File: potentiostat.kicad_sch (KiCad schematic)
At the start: 30 parts, among them J1 Conn_01x01_Socket, J2 Conn_01x01_Socket, SW1 SW_Push, SW2 SW_Push, U1 ESP32-WROOM-32, U2 AD9833xRM, U3 TLV2372ID, U4 AMS1117-3.3, Y2 25MHz

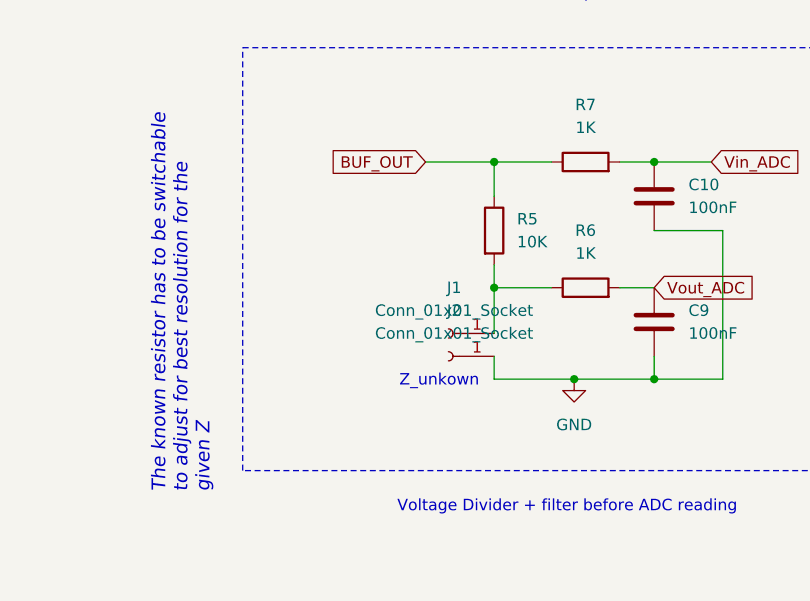
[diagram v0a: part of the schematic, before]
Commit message: dip switch added
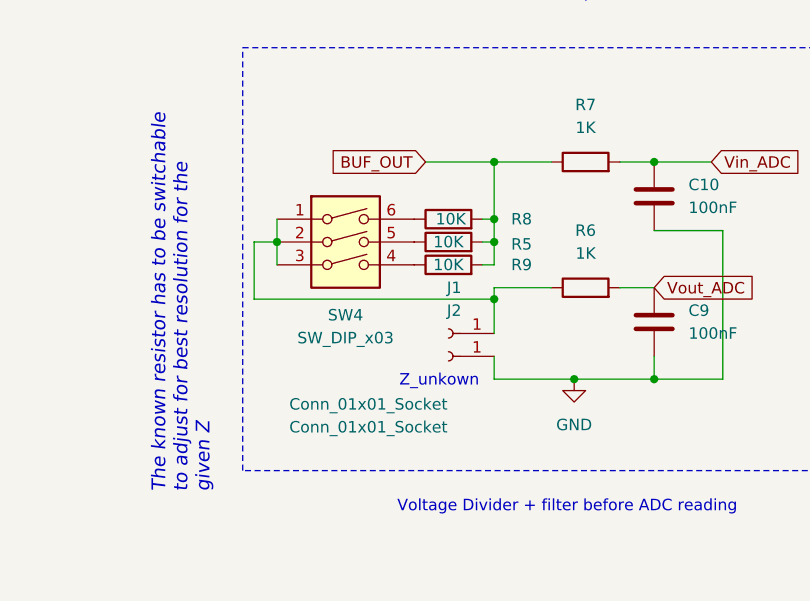
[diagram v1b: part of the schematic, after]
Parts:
- added R8, R9: 10K, Resistor_SMD:R_0603_1608Metric, symbol Device:R
- added SW4: SW_DIP_x03, Button_Switch_SMD:SW_DIP_SPSTx03_Slide_KingTek_DSHP03TJ_W5.25mm_P1.27mm_JPin, symbol Switch:SW_DIP_x03
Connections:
- net BUF_OUT: now also R5.2, R8.2, R9.2; no longer R5.1
- net at J1.1 (Pin_1), R6.1: now also SW4.1, SW4.2, SW4.3; no longer R5.2
- new net: R8.1, SW4.6
- new net: R9.1, SW4.4
- new net: R5.1, SW4.5
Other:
- moved on the sheet: R5

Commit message: debugging pins
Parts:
- added J3: Conn_01x03_Pin, Connector_PinHeader_2.54mm:PinHeader_1x03_P2.54mm_Horizontal, symbol Connector:Conn_01x03_Pin
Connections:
- net GND: now also J3.1 (Pin_1)
- net RX: now reaches U1.34 (RXD0/IO3)
- net RX: now also J3.2 (Pin_2)
- net TX: now reaches U1.35 (TXD0/IO1)
- net TX: now also J3.3 (Pin_3)
- no-connect marks 29 -> 27
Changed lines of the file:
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@@
 	)
 	(rectangle
+		(start 139.7 105.41)
+		(end 157.48 128.27)
+		(stroke
+			(width 0)
+			(type dash)
+		)
+		(fill
+			(type none)
+		)
+	)
+	(rectangle
 		(start 24.13 69.85)
 		(end 67.31 95.25)
@@
 		)
 	)
+	(rectangle
+		(start 69.85 71.12)
+		(end 91.44 93.98)
+		(stroke
+			(width 0)
+			(type dash)
+		)
+		(fill
+			(type none)
+		)
+	)
 	(text "1.65V mid bias"
 		(exclude_from_sim no)
@@
 	)
 	(no_connect
-		(at 125.73 114.3)
-	)
-	(no_connect
 		(at 95.25 116.84)
 	)
@@
 	)
 	(no_connect
-		(at 125.73 119.38)
-	)
-	(no_connect
 		(at 125.73 139.7)
 	)
@@
 		)
 	)
+	(global_label "RX"
+		(shape input)
+		(at 148.59 119.38 270)
+		(fields_autoplaced yes)
+		(effects
+			(font
+				(size 1.27 1.27)
+			)
+			(justify right)
+		)
+		(property "Intersheetrefs" "${INTERSHEET_REFS}"
+			(at 148.59 124.8447 90)
+			(effects
+				(font
+					(size 1.27 1.27)
+				)
+				(justify right)
+				(hide yes)
+			)
+		)
+	)
 	(global_label "FSYNC"
 		(shape input)
@@
 		)
 	)
+	(global_label "TX"
+		(shape input)
+		(at 125.73 114.3 0)
+		(fields_autoplaced yes)
+		(effects
+			(font
+				(size 1.27 1.27)
+			)
+			(justify left)
+		)
+		(property "Intersheetrefs" "${INTERSHEET_REFS}"
+			(at 130.8923 114.3 0)
+			(effects
+				(font
+					(size 1.27 1.27)
+				)
+				(justify left)
+				(hide yes)
+			)
+		)
+	)
 	(global_label "BOOT"
 		(shape input)
@@
 		)
 	)
+	(global_label "TX"
+		(shape input)
+		(at 146.05 119.38 270)
+		(fields_autoplaced yes)
+		(effects
+			(font
+				(size 1.27 1.27)
+			)
+			(justify right)
+		)
+		(property "Intersheetrefs" "${INTERSHEET_REFS}"
+			(at 146.05 124.5423 90)
+			(effects
+				(font
+					(size 1.27 1.27)
+				)
+				(justify right)
+				(hide yes)
+			)
+		)
+	)
 	(global_label "SPICLK"
 		(shape input)
@@
 		)
 	)
+	(global_label "RX"
+		(shape input)
+		(at 125.73 119.38 0)
+		(fields_autoplaced yes)
+		(effects
+			(font
+				(size 1.27 1.27)
+			)
+			(justify left)
+		)
+		(property "Intersheetrefs" "${INTERSHEET_REFS}"
+			(at 131.1947 119.38 0)
+			(effects
+				(font
+					(size 1.27 1.27)
+				)
+				(justify left)
+				(hide yes)
+			)
+		)
+	)
 	(global_label "Vout_ADC"
 		(shape input)
@@
 	)
 	(symbol
+		(lib_id "Connector:Conn_01x03_Pin")
+		(at 148.59 114.3 270)
+		(unit 1)
+		(exclude_from_sim no)
+		(in_bom yes)
+		(on_board yes)
+		(dnp no)
+		(fields_autoplaced yes)
+		(property "Reference" "J3"
+			(at 148.59 109.22 90)
+			(effects
+				(font
+					(size 1.27 1.27)
+				)
+			)
+		)
+		(property "Value" "Conn_01x03_Pin"
+			(at 148.59 111.76 90)
+			(effects
+				(font
+					(size 1.27 1.27)
+				)
+			)
+		)
+		(property "Footprint" "Connector_PinHeader_2.54mm:PinHeader_1x03_P2.54mm_Horizontal"
+			(at 148.59 114.3 0)
+			(effects
+				(font
+					(size 1.27 1.27)
+				)
+				(hide yes)
+			)
+		)
+		(property "Datasheet" "~"
+			(at 148.59 114.3 0)
+			(effects
+				(font
+					(size 1.27 1.27)
+				)
+				(hide yes)
+			)
+		)
+		(property "Description" "Generic connector, single row, 01x03, script generated"
+			(at 148.59 114.3 0)
+			(effects
+				(font
+					(size 1.27 1.27)
+				)
+				(hide yes)
+			)
+		)
+		(pin "2"
+		)
+		(pin "1"
+		)
+		(pin "3"
+		)
+		(instances
+			(project ""
+				(path "/ba366fb0-3100-453d-b398-5cb6fed3df38"
+					(reference "J3")
+					(unit 1)
+				)
+			)
+		)
+	)
+	(symbol
 		(lib_id "Device:R")
 		(at 204.47 38.1 0)
@@
 					(unit 1)
 				)
+			)
+		)
+	)
+	(symbol
+		(lib_id "power:GND")
+		(at 151.13 119.38 0)
+		(unit 1)
+		(exclude_from_sim no)
+		(in_bom yes)
+		(on_board yes)
+		(dnp no)
+		(fields_autoplaced yes)
+		(property "Reference" "#PWR019"
+			(at 151.13 125.73 0)
+			(effects
+				(font
+					(size 1.27 1.27)
+				)
+				(hide yes)
+			)
+		)
+		(property "Value" "GND"
+			(at 151.13 124.46 0)
+			(effects
+				(font
+					(size 1.27 1.27)
+				)
+			)
+		)
+		(property "Footprint" ""
+			(at 151.13 119.38 0)
+			(effects
+				(font
+					(size 1.27 1.27)
+				)
+				(hide yes)
+			)
+		)
+		(property "Datasheet" ""
+			(at 151.13 119.38 0)
+			(effects
+				(font
+					(size 1.27 1.27)
+				)
+				(hide yes)
+			)
+		)
+		(property "Description" "Power symbol creates a global label with name \"GND\" , ground"
+			(at 151.13 119.38 0)
+			(effects
+				(font
+					(size 1.27 1.27)
+				)
+				(hide yes)
+			)
+		)
+		(pin "1"
+		)
+		(instances
+			(project ""
+				(path "/ba366fb0-3100-453d-b398-5cb6fed3df38"
+					(reference "#PWR019")
+					(unit 1)
+				)
